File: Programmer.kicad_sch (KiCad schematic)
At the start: 44 parts, among them J1 ZIF-socket, J2 ISP, J7 ZIF_VCC, P1 USB-C, Q2 BC327, Q4 BC327, Q5 BC327, Q6 BC327, SW1 Reset, U1 ATmega1284-P, U2 MCP2221AxP, U4 LM358, U5 ULN2003, Y1 20M

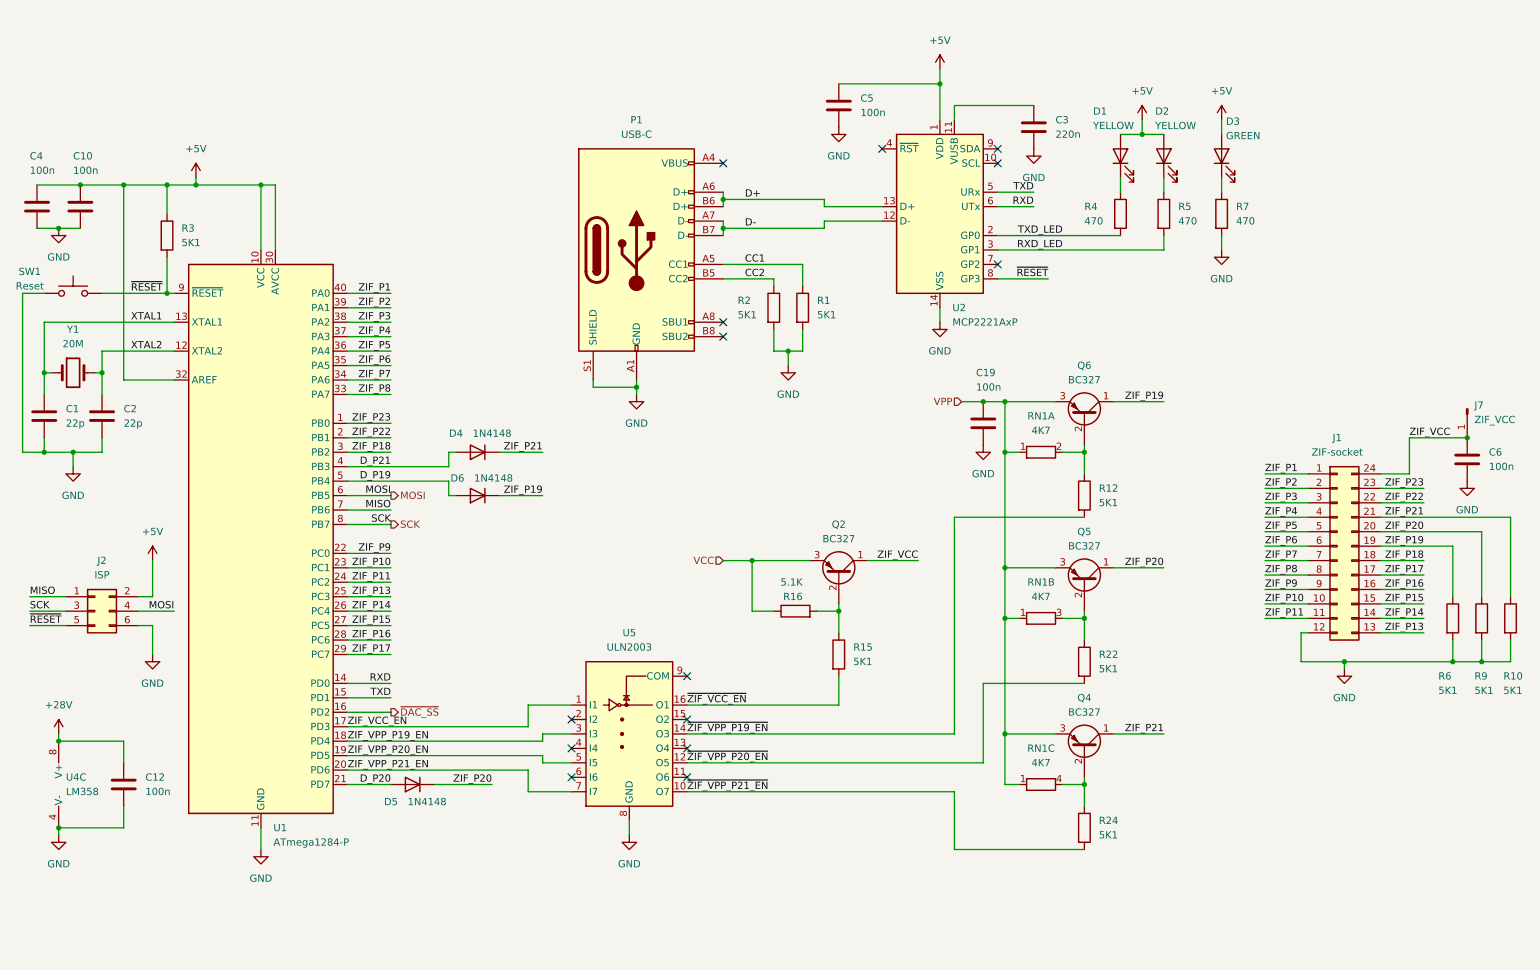
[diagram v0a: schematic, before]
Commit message: Add input/output protection on data lines (WIP)
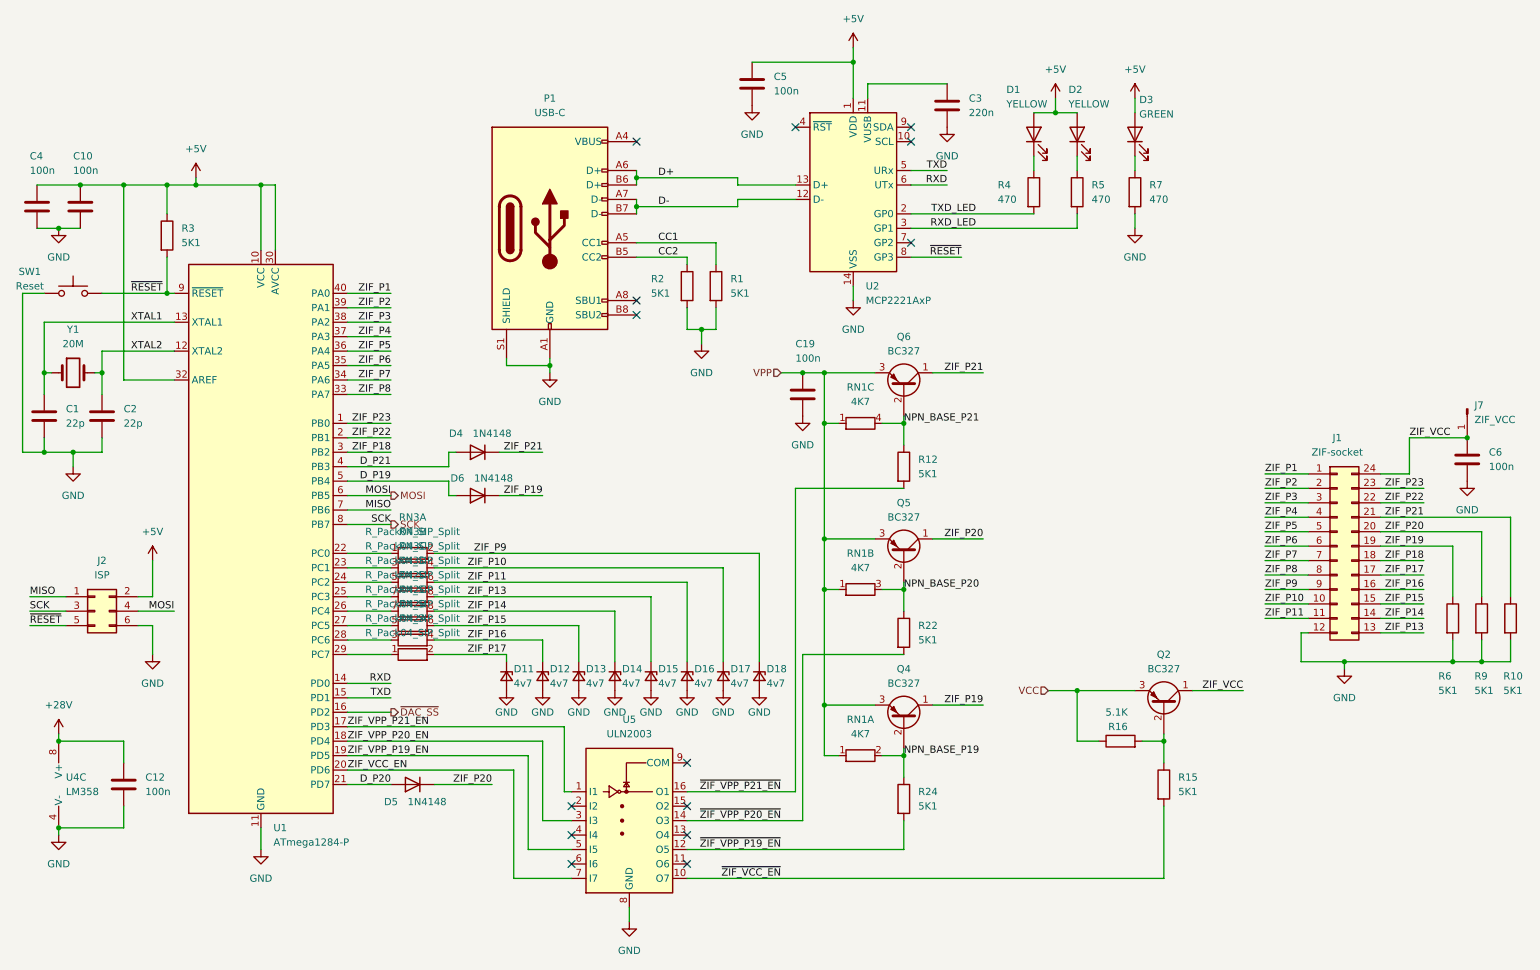
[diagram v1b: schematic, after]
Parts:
- added D11, D12, D13, D14, D15, D16, D17, D18: 4v7, Diode_THT:D_DO-35_SOD27_P7.62mm_Horizontal, symbol Device:D_Zener_Small
- added RN2, RN3: R_Pack04_SIP_Split, Resistor_THT:R_Array_SIP8, symbol Device:R_Pack04_SIP_Split
- renumbered Q6 to Q4, Q4 to Q6, R24 to R12, R12 to R24
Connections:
- net GND: now also D11.2 (A), D12.2 (A), D13.2 (A), D14.2 (A), D15.2 (A), D16.2 (A), D17.2 (A), D18.2 (A)
- net ZIF_P10: now also D17.1 (K), RN3.4 (R2.2); no longer U1.23 (PC1)
- net ZIF_P11: now also D16.1 (K), RN3.6 (R3.2); no longer U1.24 (PC2)
- net ZIF_P13: now also D15.1 (K), RN3.8 (R4.2); no longer U1.25 (PC3)
- net ZIF_P14: now also D14.1 (K), RN2.8 (R4.2); no longer U1.26 (PC4)
- net ZIF_P15: now also D13.1 (K), RN2.6 (R3.2); no longer U1.27 (PC5)
- net ZIF_P16: now also D12.1 (K), RN2.4 (R2.2); no longer U1.28 (PC6)
- net ZIF_P17: now also D11.1 (K), RN2.2 (R1.2); no longer U1.29 (PC7)
- net ZIF_P9: now also D18.1 (K), RN3.2 (R1.2); no longer U1.22 (PC0)
- net ZIF_VCC_EN: now also U1.20 (PD6), U5.7 (I7); no longer U1.17 (PD3), U5.1 (I1)
- net ZIF_VPP_P19_EN: now also U1.19 (PD5), U5.5 (I5); no longer U1.18 (PD4), U5.3 (I3)
- net ZIF_VPP_P20_EN: now also U1.18 (PD4), U5.3 (I3); no longer U1.19 (PD5), U5.5 (I5)
- net ZIF_VPP_P21_EN: now also U1.17 (PD3), U5.1 (I1); no longer U1.20 (PD6), U5.7 (I7)
- net ~{ZIF_VCC_EN}: now also U5.10 (O7); no longer U5.16 (O1)
- net ~{ZIF_VPP_P19_EN}: now also U5.12 (O5); no longer U5.14 (O3)
- net ~{ZIF_VPP_P20_EN}: now also U5.14 (O3); no longer U5.12 (O5)
- net ~{ZIF_VPP_P21_EN}: now also U5.16 (O1); no longer U5.10 (O7)
- net NPN_BASE_P21: now reaches Q6.2 (B), R12.1, RN1.4 (R3.2)
- net NPN_BASE_P20: now reaches Q5.2 (B), R22.1, RN1.3 (R2.2)
- net NPN_BASE_P19: now reaches Q4.2 (B), R24.1, RN1.2 (R1.2)
- new net: RN3.1 (R1.1), U1.22 (PC0)
- new net: RN3.3 (R2.1), U1.23 (PC1)
- new net: RN3.5 (R3.1), U1.24 (PC2)
- new net: RN3.7 (R4.1), U1.25 (PC3)
- new net: RN2.7 (R4.1), U1.26 (PC4)
- new net: RN2.5 (R3.1), U1.27 (PC5)
- new net: RN2.3 (R2.1), U1.28 (PC6)
- new net: RN2.1 (R1.1), U1.29 (PC7)
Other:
- moved on the sheet: C19, C3, C5, D1, D2, D3, P1, Q2, Q4, Q5, Q6, R1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

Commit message: Clean up of schematic
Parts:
- RN2, RN3: value R_Pack04_SIP_Split -> 120
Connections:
- net MCU_P9: now reaches RN3.1 (R1.1), U1.22 (PC0)
- net MCU_P10: now reaches RN3.3 (R2.1), U1.23 (PC1)
- net MCU_P11: now reaches RN3.5 (R3.1), U1.24 (PC2)
- net MCU_P13: now reaches RN3.7 (R4.1), U1.25 (PC3)
- net MCU_P14: now reaches RN2.7 (R4.1), U1.26 (PC4)
- net MCU_P15: now reaches RN2.5 (R3.1), U1.27 (PC5)
- net MCU_P16: now reaches RN2.3 (R2.1), U1.28 (PC6)
- net MCU_P17: now reaches RN2.1 (R1.1), U1.29 (PC7)
- net D_P19 renamed MCU_P19
- net D_P20 renamed MCU_P20
- net D_P21 renamed MCU_P21
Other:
- moved on the sheet: D11, D12, D13, D14, D15, D16, D17, D18, D5, RN2A, RN3A

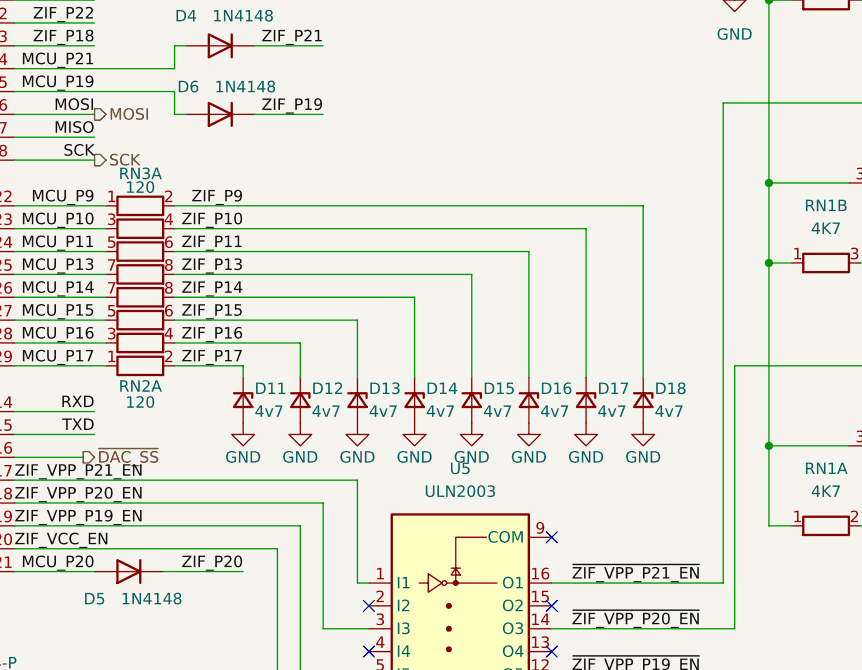
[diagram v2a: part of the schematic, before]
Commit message: Finish input/output protection on data lines
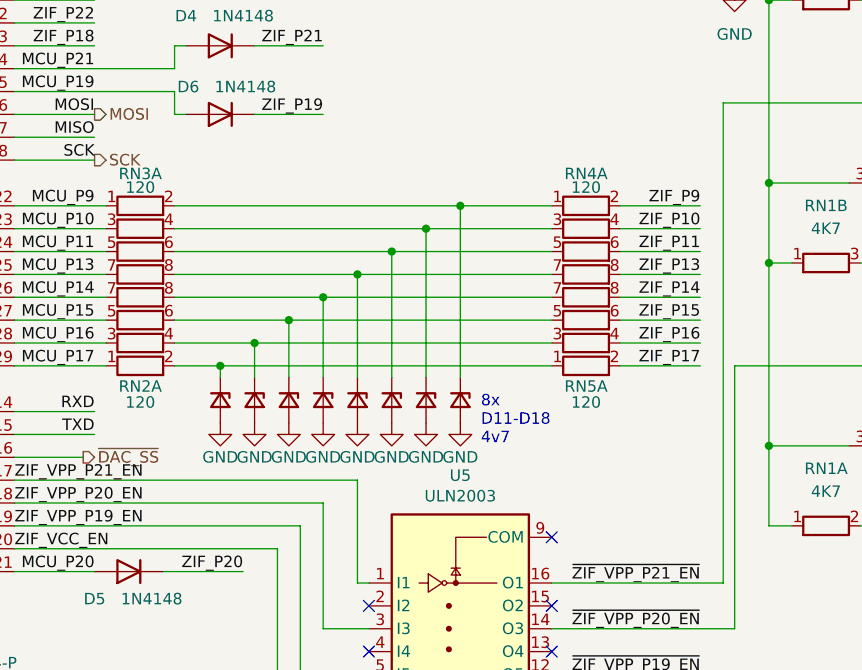
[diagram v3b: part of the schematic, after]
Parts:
- added RN4, RN5: 120, Resistor_THT:R_Array_SIP8, symbol Device:R_Pack04_SIP_Split
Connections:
- net ZIF_P10: now also RN4.4 (R2.2); no longer D17.1 (K), RN3.4 (R2.2)
- net ZIF_P11: now also RN4.6 (R3.2); no longer D16.1 (K), RN3.6 (R3.2)
- net ZIF_P13: now also RN4.8 (R4.2); no longer D15.1 (K), RN3.8 (R4.2)
- net ZIF_P14: now also RN5.8 (R4.2); no longer D14.1 (K), RN2.8 (R4.2)
- net ZIF_P15: now also RN5.6 (R3.2); no longer D13.1 (K), RN2.6 (R3.2)
- net ZIF_P16: now also RN5.4 (R2.2); no longer D12.1 (K), RN2.4 (R2.2)
- net ZIF_P17: now also RN5.2 (R1.2); no longer D11.1 (K), RN2.2 (R1.2)
- net ZIF_P9: now also RN4.2 (R1.2); no longer D18.1 (K), RN3.2 (R1.2)
- new net: D13.1 (K), RN2.6 (R3.2), RN5.5 (R3.1)
- new net: D11.1 (K), RN2.2 (R1.2), RN5.1 (R1.1)
- new net: D14.1 (K), RN2.8 (R4.2), RN5.7 (R4.1)
- new net: D17.1 (K), RN3.4 (R2.2), RN4.3 (R2.1)
- new net: D18.1 (K), RN3.2 (R1.2), RN4.1 (R1.1)
- new net: D12.1 (K), RN2.4 (R2.2), RN5.3 (R2.1)
- new net: D15.1 (K), RN3.8 (R4.2), RN4.7 (R4.1)
- new net: D16.1 (K), RN3.6 (R3.2), RN4.5 (R3.1)
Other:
- note added: "8x D11-D18 4v7"

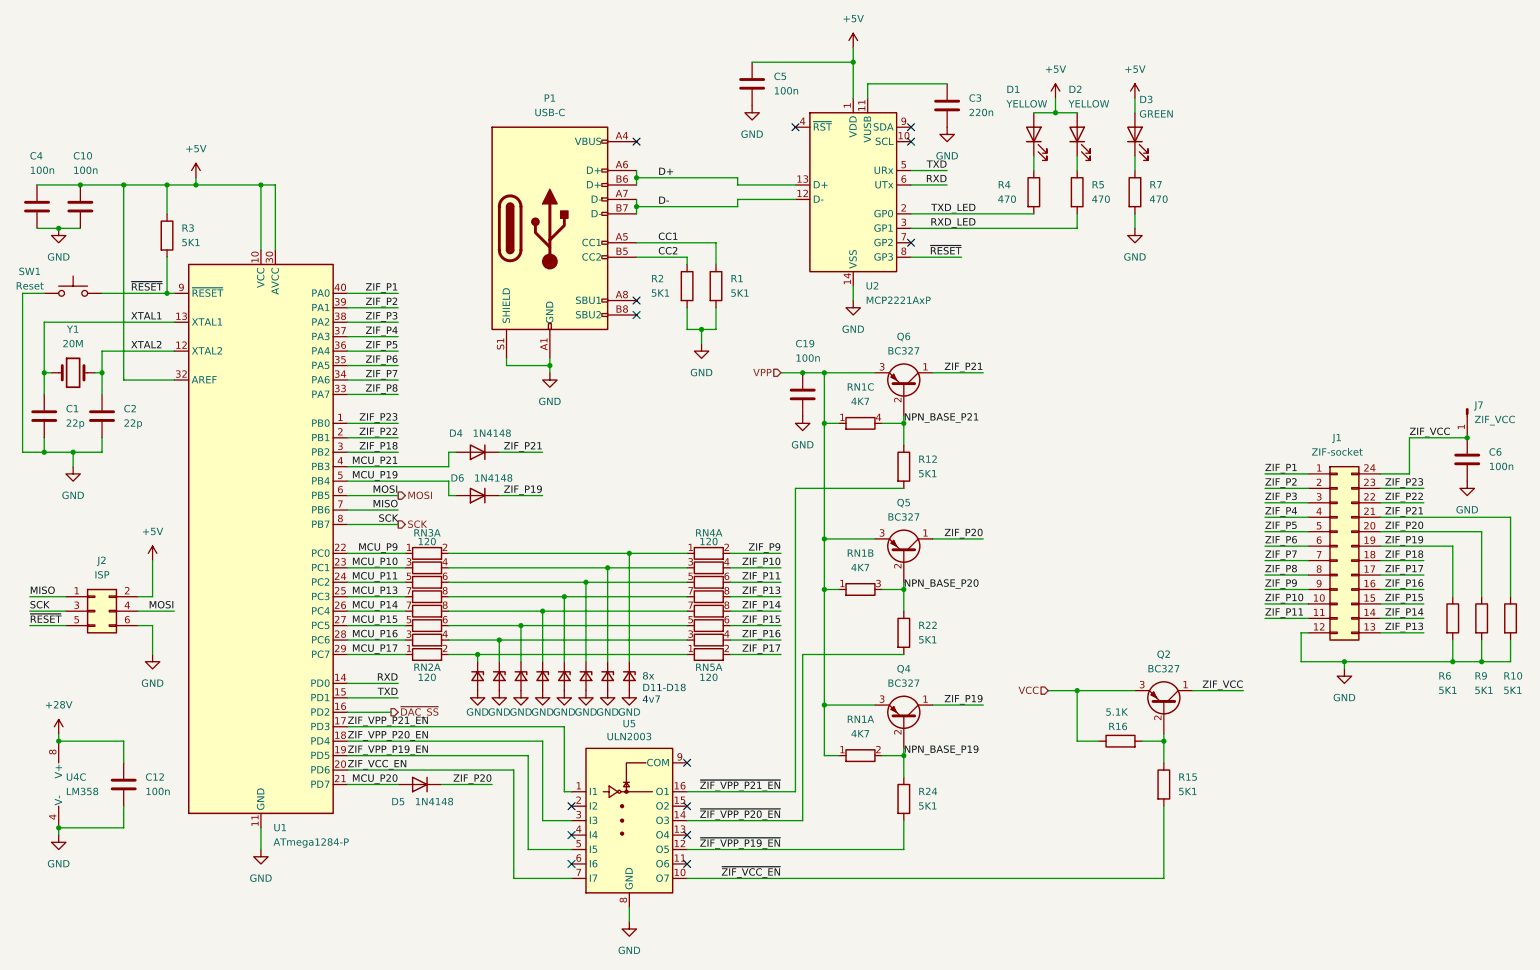
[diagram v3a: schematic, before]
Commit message: Add aditional filter for 28v line
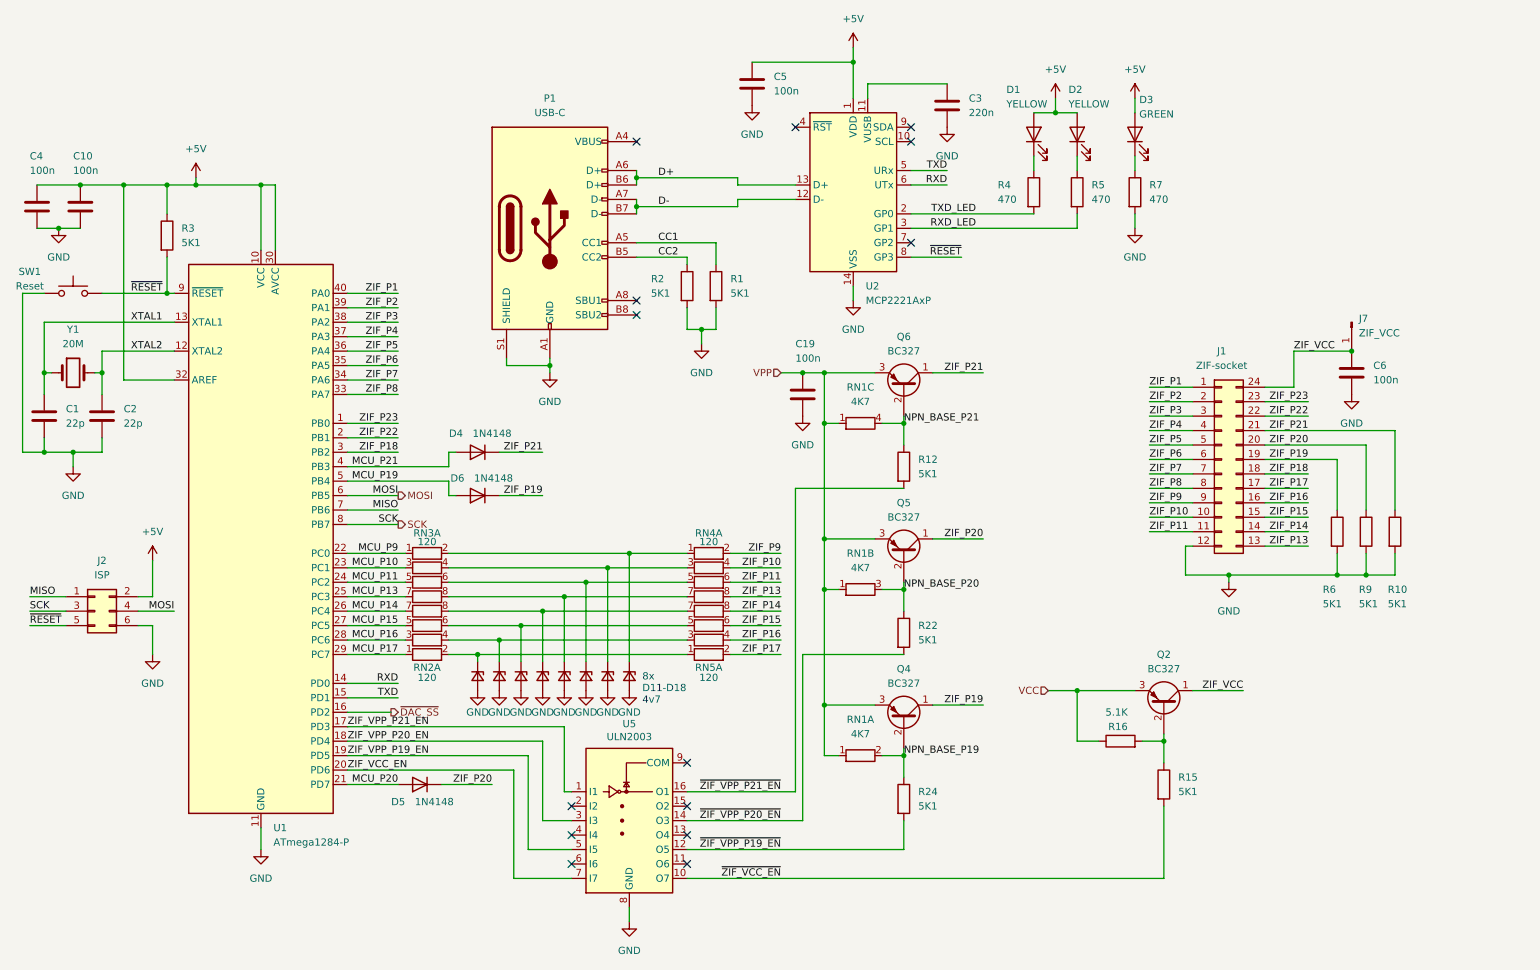
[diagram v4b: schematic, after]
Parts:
- removed C12: 100n, Capacitor_THT:C_Rect_L4.6mm_W3.0mm_P2.50mm_MKS02_FKP02, symbol Device:C
- removed U4: LM358, Package_DIP:DIP-8_W7.62mm_Socket, symbol Amplifier_Operational:LM358
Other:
- moved on the sheet: C6, J1, J7, R10, R6, R9

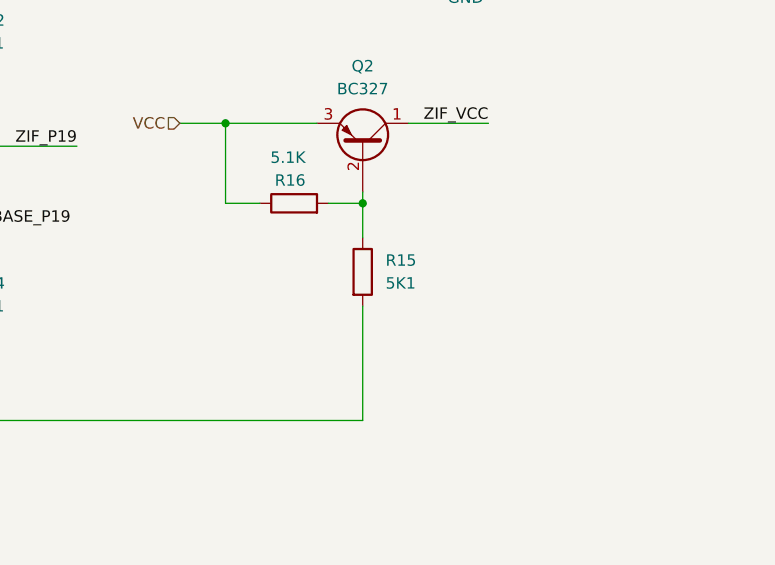
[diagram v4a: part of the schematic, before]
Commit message: Increase base current to VCC transistor
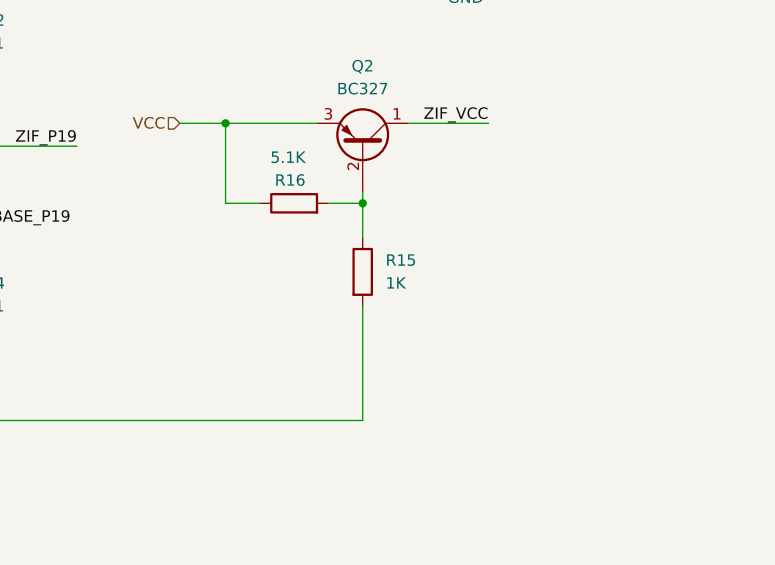
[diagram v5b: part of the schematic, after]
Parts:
- R15: value 5K1 -> 1K
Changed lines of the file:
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@@
 			)
 		)
-		(property "Value" "5K1"
+		(property "Value" "1K"
 			(at 219.71 149.86 0)
 			(effects
